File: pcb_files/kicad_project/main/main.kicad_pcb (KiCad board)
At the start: 2 copper layers, 102 x 90.8 mm, 252 parts, among them IC1 AS5145B-HSST, IC2 AS5145B-HSST, J1 Conn_01x02_Socket, J2 Conn_01x04_Socket, Q1 AON7423, Y1 Crystal_GND24

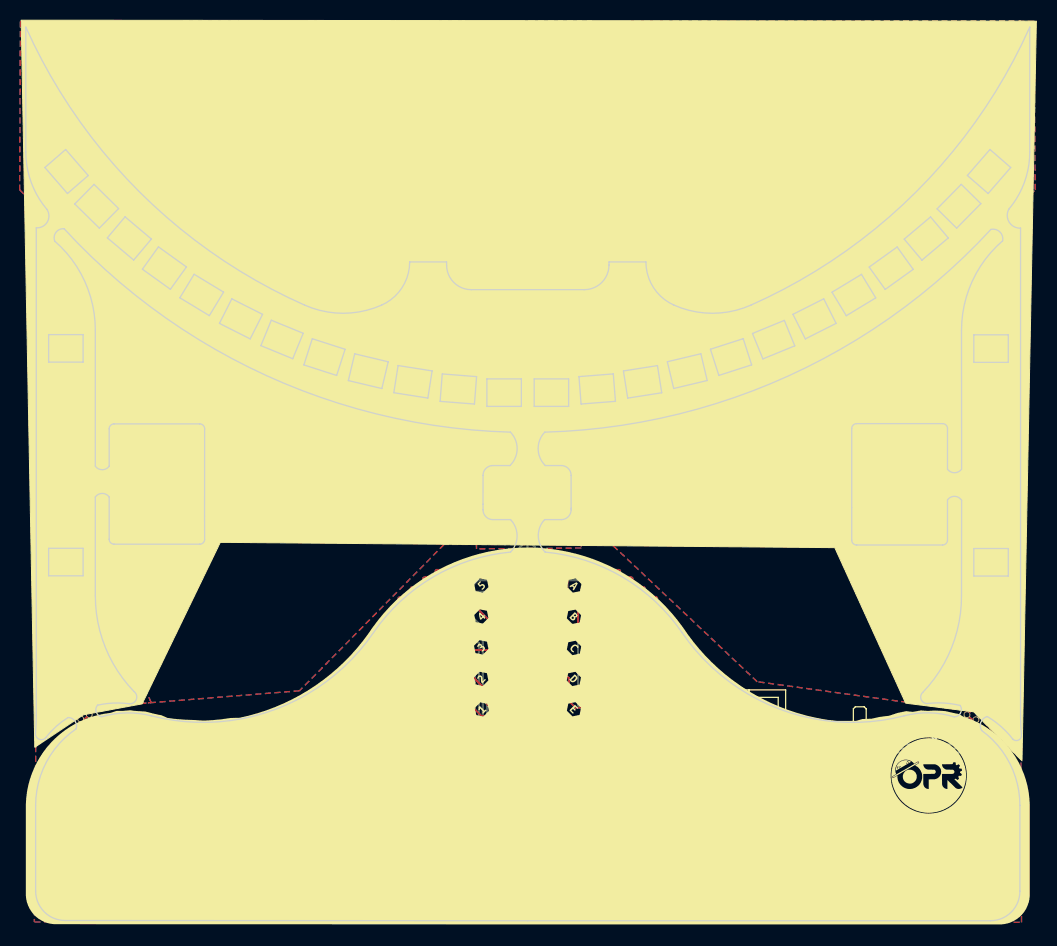
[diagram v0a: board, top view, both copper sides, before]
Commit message: Termina ruteo de la rebuild.
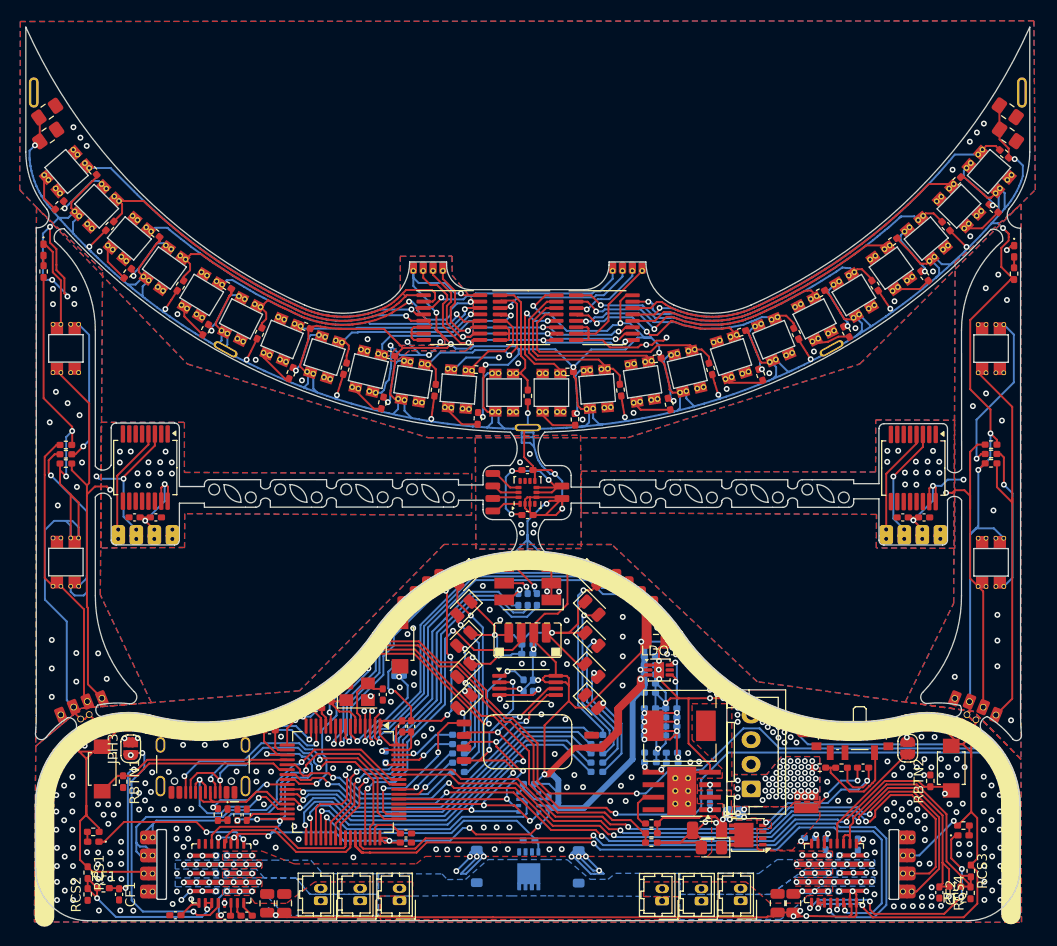
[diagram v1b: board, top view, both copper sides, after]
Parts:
- removed the ? at (191.0, 62.9)
- removed the ? at (193.6, 124.9)
- removed the ? at (97.9, 62.9)
- removed the ? at (95.2, 124.9)
- removed CM1, CM11, CM3, CM5, CM7, CM9: 10uF, Capacitor_SMD:C_0402_1005Metric_Pad0.74x0.62mm_HandSolder
- removed CM10, CM12, CM2, CM4, CM6, CM8: 0.1uF, Capacitor_SMD:C_0402_1005Metric_Pad0.74x0.62mm_HandSolder
- added BTN_MENU1: ~, custom_footprints:Generic_SmallButton_6x3, F.Cu at (101.1, 113.8)
- added BTN_MENU2: ~, custom_footprints:Generic_SmallButton_6x3, F.Cu at (187.4, 113.7)
- added CF1: 0.22uF, Capacitor_SMD:C_0402_1005Metric_Pad0.74x0.62mm_HandSolder, F.Cu at (102.9, 126.5)
- added CF2: 0.22uF, Capacitor_SMD:C_0402_1005Metric_Pad0.74x0.62mm_HandSolder, F.Cu at (186.2, 126.3)
- added JPH2: JPH2, Jumper:SolderJumper-2_P1.3mm_Open_RoundedPad1.0x1.5mm, F.Cu at (183.0, 111.6)
- added JPH3: JPH2, Jumper:SolderJumper-2_P1.3mm_Open_RoundedPad1.0x1.5mm, F.Cu at (104.0, 111.7)
- added RBTN1: 47k, Resistor_SMD:R_0402_1005Metric_Pad0.72x0.64mm_HandSolder, F.Cu at (103.3, 115.0)
- added RBTN2: 47k, Resistor_SMD:R_0402_1005Metric_Pad0.72x0.64mm_HandSolder, F.Cu at (185.3, 115.0)
- added RCS1: 5K, Resistor_SMD:R_0402_1005Metric_Pad0.72x0.64mm_HandSolder, F.Cu at (99.7, 124.3)
- added RCS2: 5K, Resistor_SMD:R_0402_1005Metric_Pad0.72x0.64mm_HandSolder, F.Cu at (99.7, 126.5)
- added RCS3: 5K, Resistor_SMD:R_0402_1005Metric_Pad0.72x0.64mm_HandSolder, F.Cu at (189.4, 124.1)
- added RCS4: 5K, Resistor_SMD:R_0402_1005Metric_Pad0.72x0.64mm_HandSolder, F.Cu at (189.4, 126.3)
- added RF1: 220, Resistor_SMD:R_0402_1005Metric_Pad0.72x0.64mm_HandSolder, F.Cu at (101.3, 125.9)
- added RF2: 220, Resistor_SMD:R_0402_1005Metric_Pad0.72x0.64mm_HandSolder, F.Cu at (187.8, 125.7)
- BMP1: value ~ -> BMP280
- CONN_ENC_L1, CONN_ENC_R1: footprint custom_footprints:DragonBot2_Encoder_main -> custom_footprints:DragonBot_PCBmodule_encoder
- ENC_L1, ENC_R1: footprint custom_footprints:DragonBot2_Encoder_main -> custom_footprints:DragonBot2_PCBmain_Encoder
- LDO1: value ~ -> LDL212PV33R; footprint Package_DFN_QFN:DFN-6-1EP_3x3mm_P0.95mm_EP1.7x2.6mm -> custom_footprints:DFN-6-2x2mm_P0.5mm_LDO_Dragonbot
- moved RPH2 4.67 mm to (188.6, 119.5)
- moved RPH1 4.54 mm to (100.2, 120.1)
- moved DPH1 3.09 mm to (100.2, 121.1)
- moved DPH2 2.88 mm to (188.6, 120.5)
- moved CONN_ENC_L1 1.52 mm to (183.5, 89.9), turned to 180 degrees
- moved IC1 1.43 mm to (183.5, 83.2)
- moved CEN1 1.38 mm to (184.6, 88.2)
- moved CEN2 1.38 mm to (182.5, 88.2)
- moved CONN_ENC_R1 1.28 mm to (105.5, 89.9), turned to 180 degrees
- moved CEN3 1.20 mm to (106.6, 88.2)
- moved CEN4 1.20 mm to (104.4, 88.2)
- moved IC2 1.19 mm to (105.5, 83.1)
- moved CPH3 0.98 mm to (108.6, 128.6)
- moved LDO1 0.06 mm to (157.7, 103.7)
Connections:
- ARRAY_MORRO1 pad 2: /OUT_MUX_A -> /IN_MUX_A
- ARRAY_MORRO1 pad 3: /OUT_MUX_B -> /IN_MUX_B
- ARRAY_MORRO1 pad 4: /OUT_MUX_C -> /IN_MUX_C
- ARRAY_MORRO1 pad 5: /IN_LIN_A -> /OUT_CH_A
- ARRAY_MORRO1 pad 6: /IN_LIN_B -> /OUT_CH_B
- ARRAY_MORRO1 pad 7: /IN_LIN_C -> /OUT_CH_C
- DEIXAME_QUE_PENSE_1 pad 10: /IN_LIN_C -> /IN_MUX_A
- DEIXAME_QUE_PENSE_1 pad 2: /OUT_MUX_C -> /OUT_CH_C
- DEIXAME_QUE_PENSE_1 pad 20: /IN_CURR_ML_A -> /CURR_SEN_ML
- DEIXAME_QUE_PENSE_1 pad 21: /IN_CURR_ML_B -> /CURR_SEN_MR
- DEIXAME_QUE_PENSE_1 pad 22: /IN_CURR_MR_A -> /MENU_BTN_L
- DEIXAME_QUE_PENSE_1 pad 23: /IN_CURR_MR_B -> /MENU_BTN_R
- DEIXAME_QUE_PENSE_1 pad 3: /OUT_MUX_B -> /OUT_CH_B
- DEIXAME_QUE_PENSE_1 pad 4: /OUT_MUX_A -> /OUT_CH_A
- DEIXAME_QUE_PENSE_1 pad 56: /ENC_L_A -> /ENC_L_B
- DEIXAME_QUE_PENSE_1 pad 57: /ENC_L_B -> /ENC_L_A
- DEIXAME_QUE_PENSE_1 pad 8: /IN_LIN_A -> /IN_MUX_C
- DEIXAME_QUE_PENSE_1 pad 9: /IN_LIN_B -> /IN_MUX_B
- IC1 pad 1: /Sensores/MARK_L1 -> unconnected-(IC1-MAGINCN-Pad1)
- IC2 pad 8: /Sensores/MARK_R2 -> unconnected-(IC2-PDIO-Pad8)
- J1 pad 1: +3V3 -> /3.3_MPU
- MP1 pad 15: /IN_CURR_ML_A -> Net-(MP1-SOA)
- MP1 pad 16: /IN_CURR_ML_B -> Net-(MP1-SOA)
- MP1 pad 17: GND -> Net-(JPH3-A)
- MP2 pad 15: /IN_CURR_MR_A -> Net-(MP2-SOA)
- MP2 pad 16: /IN_CURR_MR_B -> Net-(MP2-SOA)
- MP2 pad 17: GND -> Net-(JPH2-A)
- POWER_SWITCH1 pad : GND -> (no net)
- R18 pad 1: /Sensores/3.3_M -> /Sensores/3.3_ML
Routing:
- net /CURR_SEN_MR: track 0.00 -> 86.4 mm, vias 0 -> 4
- net /MENU_BTN_R: track 0.00 -> 74.7 mm, vias 0 -> 4
- net /IN_CURR_MR_A: track 66.1 -> 0.00 mm, vias 4 -> 0
- net /IN_CURR_MR_B: track 64.0 -> 0.00 mm, vias 4 -> 0
- net /IN_LIN_C: track 45.5 -> 0.00 mm, vias 1 -> 0
- net /IN_LIN_B: track 43.3 -> 0.00 mm, vias 1 -> 0
- net /OUT_CH_C: track 0.00 -> 42.2 mm, vias 0 -> 2
- net /OUT_CH_B: track 0.00 -> 41.4 mm, vias 0 -> 2
- net /IN_LIN_A: track 41.3 -> 0.00 mm, vias 1 -> 0
- net /OUT_CH_A: track 0.00 -> 40.2 mm, vias 0 -> 2
- net /IN_CURR_ML_A: track 39.9 -> 0.00 mm, vias 2 -> 0
- net /IN_CURR_ML_B: track 39.4 -> 0.00 mm, vias 2 -> 0
- net /CURR_SEN_ML: track 0.00 -> 30.2 mm, vias 0 -> 2
- net Net-(MP2-SOA): track 0.00 -> 29.7 mm
- net Net-(JPH3-A): track 0.00 -> 27.0 mm, vias 0 -> 3
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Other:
- outline, holes or cut-outs redrawn

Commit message: Corrige algunos errores, finaliza la serigrafía y genera los gerbes.
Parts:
- added G***: LOGO, LOGO, F.Cu at (144.1, 121.5)
- added kibuzzard-6A86F9E9: G***, kibuzzard-6A86F9E9, F.Cu at (139.5, 95.1)
- added kibuzzard-6A86F9FA: G***, kibuzzard-6A86F9FA, F.Cu at (139.5, 98.3)
- added kibuzzard-6A86FA0A: G***, kibuzzard-6A86FA0A, F.Cu at (139.5, 101.5)
- added kibuzzard-6A86FA24: G***, kibuzzard-6A86FA24, F.Cu at (139.5, 104.6)
- added kibuzzard-6A86FA32: G***, kibuzzard-6A86FA32, F.Cu at (139.5, 107.8)
- added kibuzzard-6A86FBBC: G***, kibuzzard-6A86FBBC, F.Cu at (149.2, 107.7)
- added kibuzzard-6A86FBC4: G***, kibuzzard-6A86FBC4, F.Cu at (149.2, 104.5)
- added kibuzzard-6A86FBCD: G***, kibuzzard-6A86FBCD, F.Cu at (149.2, 101.4)
- added kibuzzard-6A86FBEE: G***, kibuzzard-6A86FBEE, F.Cu at (149.2, 98.2)
- added kibuzzard-6A86FBF6: G***, kibuzzard-6A86FBF6, F.Cu at (149.2, 95.1)
- turned S10 to 98.9 degrees
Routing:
- net /Sensores/MARK_L1: track 34.2 -> 32.4 mm
- net /OUT_CH_C: track 42.2 -> 40.4 mm, vias 2 -> 1
- net /OUT_CH_B: track 41.4 -> 39.8 mm, vias 2 -> 1
- net /OUT_CH_A: track 40.2 -> 38.6 mm, vias 2 -> 1
